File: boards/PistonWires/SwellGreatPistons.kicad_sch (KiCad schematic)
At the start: 47 parts, among them J1 GreatLEDs, J2 SwellLEDs, J3 GreatPistons, J4 SwellPistons, SW1 SW, SW10 SW, SW11 SW, SW12 SW, SW13 SW, SW14 SW, SW15 SW, SW16 SW, SW17 SW, SW18 SW, SW19 SW, SW20 SW, SW21 SW, SW22 SW, SW23 SW, SW24 SW, SW25 SW, SW26 SW, SW27 SW, SW28 SW, SW29 SW, SW3 SW, SW30 SW, SW31 SW, SW32 SW, SW33 SW, SW34 SW, SW35 SW, SW36 SW, SW37 SW, SW38 SW, SW39 SW, SW4 SW, SW40 SW, SW41 SW, SW42 SW, SW43 SW, SW44 SW, SW5 SW, SW6 SW, SW7 SW, SW8 SW, SW9 SW

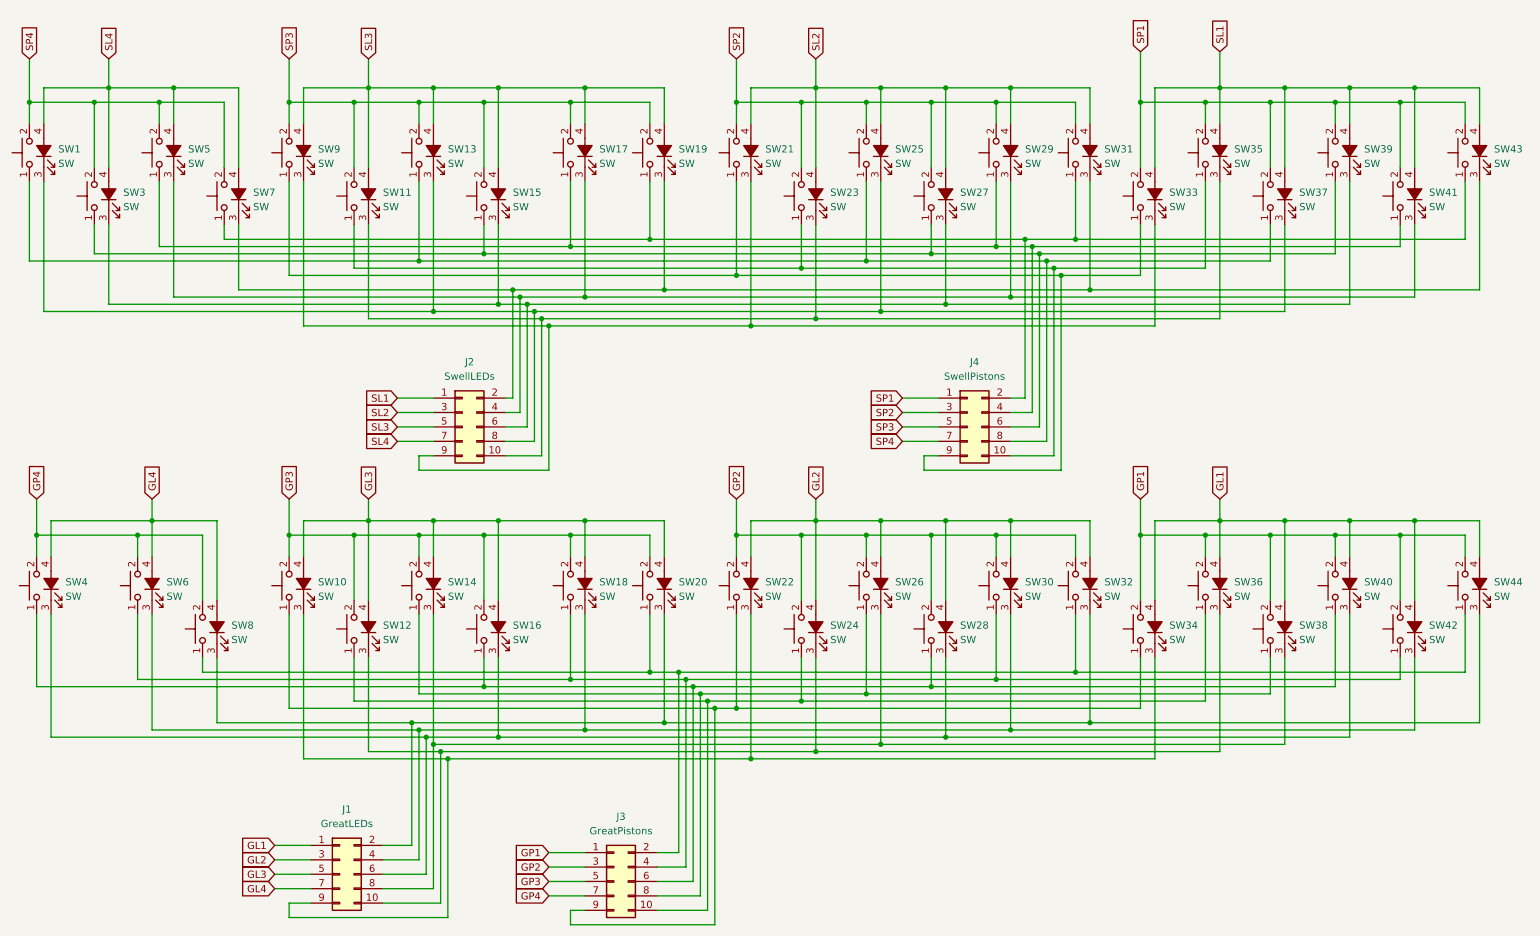
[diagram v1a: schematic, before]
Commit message: Updated to KiCAD 8, fixed optocouplers for MIDI and added powersupplies
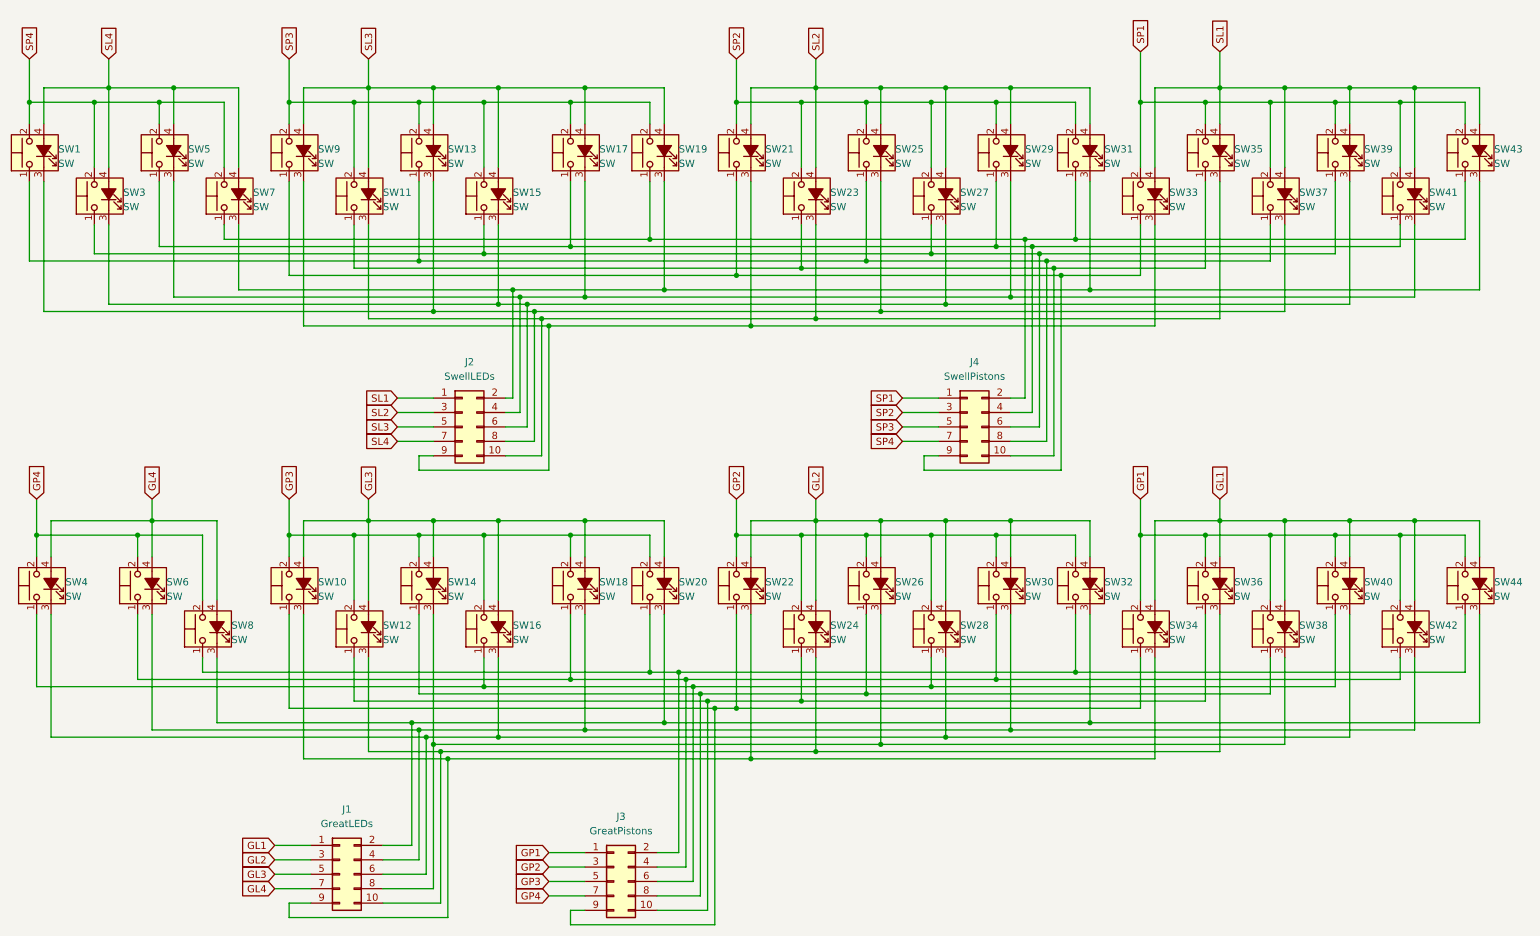
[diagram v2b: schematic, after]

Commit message: Fixed Piston wiring schematics, updated I2C message formats
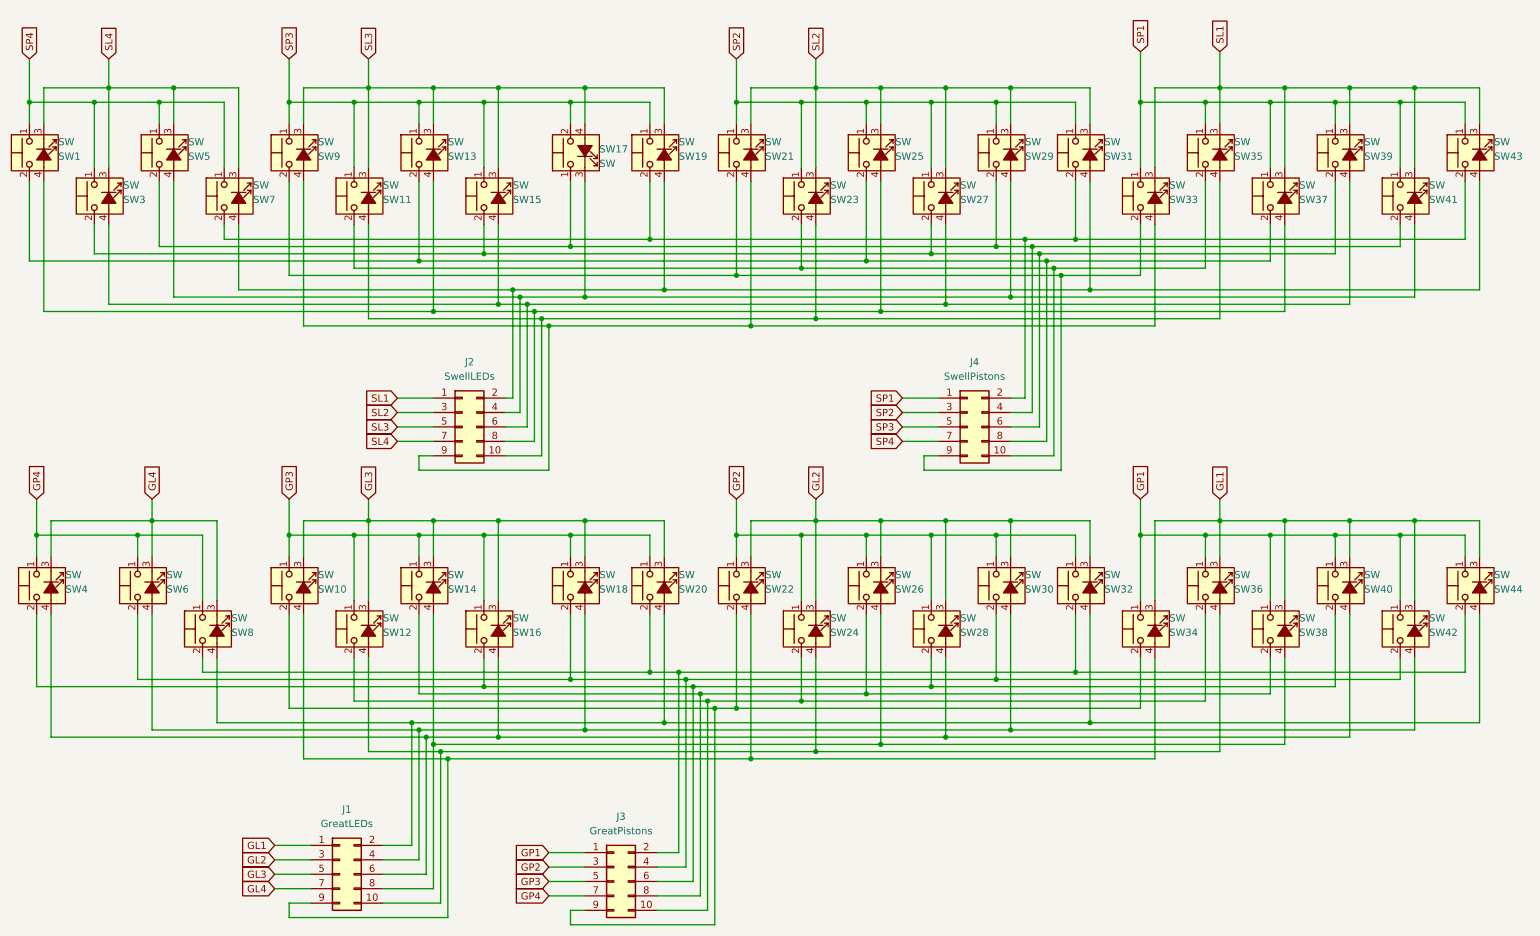
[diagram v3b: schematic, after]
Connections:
- net GL1: now also SW34.3 (K), SW36.3 (K), SW38.3 (K), SW40.3 (K), SW42.3 (K), SW44.3 (K); no longer SW34.4 (A), SW36.4 (A), SW38.4 (A), SW40.4 (A), SW42.4 (A), SW44.4 (A)
- net GL2: now also SW22.3 (K), SW24.3 (K), SW26.3 (K), SW28.3 (K), SW30.3 (K), SW32.3 (K); no longer SW22.4 (A), SW24.4 (A), SW26.4 (A), SW28.4 (A), SW30.4 (A), SW32.4 (A)
- net GL3: now also SW10.3 (K), SW12.3 (K), SW14.3 (K), SW16.3 (K), SW18.3 (K), SW20.3 (K); no longer SW10.4 (A), SW12.4 (A), SW14.4 (A), SW16.4 (A), SW18.4 (A), SW20.4 (A)
- net GL4: now also SW4.3 (K), SW6.3 (K), SW8.3 (K); no longer SW4.4 (A), SW6.4 (A), SW8.4 (A)
- net GP1: now also SW34.1, SW36.1, SW38.1, SW40.1, SW42.1, SW44.1; no longer SW34.2, SW36.2, SW38.2, SW40.2, SW42.2, SW44.2
- net GP2: now also SW22.1, SW24.1, SW26.1, SW28.1, SW30.1, SW32.1; no longer SW22.2, SW24.2, SW26.2, SW28.2, SW30.2, SW32.2
- net GP3: now also SW10.1, SW12.1, SW14.1, SW16.1, SW18.1, SW20.1; no longer SW10.2, SW12.2, SW14.2, SW16.2, SW18.2, SW20.2
- net GP4: now also SW4.1, SW6.1, SW8.1; no longer SW4.2, SW6.2, SW8.2
- net SL1: now also SW33.3 (K), SW35.3 (K), SW37.3 (K), SW39.3 (K), SW41.3 (K), SW43.3 (K); no longer SW33.4 (A), SW35.4 (A), SW37.4 (A), SW39.4 (A), SW41.4 (A), SW43.4 (A)
- net SL2: now also SW21.3 (K), SW23.3 (K), SW25.3 (K), SW27.3 (K), SW29.3 (K), SW31.3 (K); no longer SW21.4 (A), SW23.4 (A), SW25.4 (A), SW27.4 (A), SW29.4 (A), SW31.4 (A)
- net SL3: now also SW11.3 (K), SW13.3 (K), SW15.3 (K), SW19.3 (K), SW9.3 (K); no longer SW11.4 (A), SW13.4 (A), SW15.4 (A), SW19.4 (A), SW9.4 (A)
- net SL4: now also SW1.3 (K), SW3.3 (K), SW5.3 (K), SW7.3 (K); no longer SW1.4 (A), SW3.4 (A), SW5.4 (A), SW7.4 (A)
- net SP1: now also SW33.1, SW35.1, SW37.1, SW39.1, SW41.1, SW43.1; no longer SW33.2, SW35.2, SW37.2, SW39.2, SW41.2, SW43.2
- net SP2: now also SW21.1, SW23.1, SW25.1, SW27.1, SW29.1, SW31.1; no longer SW21.2, SW23.2, SW25.2, SW27.2, SW29.2, SW31.2
- net SP3: now also SW11.1, SW13.1, SW15.1, SW19.1, SW9.1; no longer SW11.2, SW13.2, SW15.2, SW19.2, SW9.2
- net SP4: now also SW1.1, SW3.1, SW5.1, SW7.1; no longer SW1.2, SW3.2, SW5.2, SW7.2
- new net: J3.9 (Pin_9), SW10.2, SW22.2, SW34.2
- new net: J1.9 (Pin_9), SW10.4 (A), SW22.4 (A), SW34.4 (A)
- new net: J4.6 (Pin_6), SW15.2, SW27.2, SW3.2, SW39.2
- new net: J2.6 (Pin_6), SW15.4 (A), SW27.4 (A), SW3.4 (A), SW39.4 (A)
- new net: J3.2 (Pin_2), SW20.2, SW32.2, SW44.2, SW8.2
- new net: J1.2 (Pin_2), SW20.4 (A), SW32.4 (A), SW44.4 (A), SW8.4 (A)
- new net: J3.6 (Pin_6), SW16.2, SW28.2, SW4.2, SW40.2
- new net: J1.6 (Pin_6), SW16.4 (A), SW28.4 (A), SW4.4 (A), SW40.4 (A)
- new net: J3.8 (Pin_8), SW14.2, SW26.2, SW38.2
- new net: J1.8 (Pin_8), SW14.4 (A), SW26.4 (A), SW38.4 (A)
- new net: J4.10 (Pin_10), SW11.2, SW23.2, SW35.2
- new net: J4.2 (Pin_2), SW19.2, SW31.2, SW43.2, SW7.2
- new net: J4.4 (Pin_4), SW17.1, SW29.2, SW41.2, SW5.2
- new net: J4.8 (Pin_8), SW1.2, SW13.2, SW25.2, SW37.2
- new net: J4.9 (Pin_9), SW21.2, SW33.2, SW9.2
- new net: J2.10 (Pin_10), SW11.4 (A), SW23.4 (A), SW35.4 (A)
- new net: J2.2 (Pin_2), SW19.4 (A), SW31.4 (A), SW43.4 (A), SW7.4 (A)
- new net: J2.4 (Pin_4), SW17.3 (K), SW29.4 (A), SW41.4 (A), SW5.4 (A)
- new net: J2.8 (Pin_8), SW1.4 (A), SW13.4 (A), SW25.4 (A), SW37.4 (A)
- new net: J2.9 (Pin_9), SW21.4 (A), SW33.4 (A), SW9.4 (A)
- new net: J3.10 (Pin_10), SW12.2, SW24.2, SW36.2
- new net: J1.10 (Pin_10), SW12.4 (A), SW24.4 (A), SW36.4 (A)
- new net: J3.4 (Pin_4), SW18.2, SW30.2, SW42.2, SW6.2
- new net: J1.4 (Pin_4), SW18.4 (A), SW30.4 (A), SW42.4 (A), SW6.4 (A)
